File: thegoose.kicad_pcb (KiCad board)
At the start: 2 copper layers, 67 x 50 mm, 45 parts, among them U1 DRV8848, U2 DRV8848, U3 DRV8848, U4 AP64500SP-13

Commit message: Newify layout
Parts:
- removed R10, R11, R12, R7, R8, R9: .33, Resistor_SMD:R_0805_2012Metric_Pad1.20x1.40mm_HandSolder
- BT1: value XT30_SOLDER_CABLE -> XT60; footprint hexy:XT30_SolderPads_1x02_P5.00mm -> hexy:AMASS_XT60PW-M_1x02_P7.20mm_Horizontal
- moved S1 78.1 mm to (179.6, 117.8), turned to -90 degrees
- moved S6 76.3 mm to (128.8, 117.8), turned to -90 degrees
- moved C10 73.8 mm to (245.6, 74.0)
- moved C11 73.8 mm to (247.8, 74.0)
- moved C13 73.8 mm to (241.6, 73.7)
- moved C6 73.8 mm to (231.8, 73.7)
- moved C7 73.8 mm to (229.6, 73.7)
- moved C9 73.8 mm to (225.8, 73.7)
- moved C1 73.6 mm to (98.8, 99.6)
- moved C3 71.3 mm to (213.0, 73.2)
- moved C4 71.3 mm to (210.8, 73.2)
- moved M1 66.6 mm to (181.8, 54.0), turned to 180 degrees
- moved S2 66.3 mm to (169.4, 117.8), turned to -90 degrees
- moved S5 65.1 mm to (138.9, 117.8), turned to -90 degrees
- moved S3 59.3 mm to (159.3, 117.8), turned to -90 degrees
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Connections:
- U1 pad 10: /ESP_D4 -> /ESP_D16
- U1 pad 15: /ESP_D16 -> /ESP_D4
- U1 pad 16: /ESP_D17 -> /ESP_D15
- U1 pad 2: Net-(M2-OUT1) -> Net-(M1-OUT1)
- U1 pad 3: Net-(U1-AISEN) -> unconnected-(U1-AISEN-Pad3)
- U1 pad 4: Net-(M2-OUT2) -> Net-(M1-OUT2)
- U1 pad 5: Net-(M1-OUT1) -> Net-(M2-OUT1)
- U1 pad 6: Net-(U1-BISEN) -> unconnected-(U1-BISEN-Pad6)
- U1 pad 7: Net-(M1-OUT2) -> Net-(M2-OUT2)
- U1 pad 9: /ESP_D15 -> /ESP_D17
- U2 pad 10: /ESP_D18 -> /ESP_D19
- U2 pad 15: /ESP_D19 -> /ESP_D18
- U2 pad 16: /ESP_D21 -> /ESP_D5
- U2 pad 2: Net-(M4-OUT1) -> Net-(M3-OUT1)
- U2 pad 3: Net-(U2-AISEN) -> unconnected-(U2-AISEN-Pad3)
- U2 pad 4: Net-(M4-OUT2) -> Net-(M3-OUT2)
- U2 pad 5: Net-(M3-OUT1) -> Net-(M4-OUT1)
- U2 pad 6: Net-(U2-BISEN) -> unconnected-(U2-BISEN-Pad6)
- U2 pad 7: Net-(M3-OUT2) -> Net-(M4-OUT2)
- U2 pad 9: /ESP_D5 -> /ESP_D21
- U3 pad 2: Net-(M6-OUT1) -> Net-(M5-OUT1)
- U3 pad 3: Net-(U3-AISEN) -> unconnected-(U3-AISEN-Pad3)
- U3 pad 4: Net-(M6-OUT2) -> Net-(M5-OUT2)
- U3 pad 5: Net-(M5-OUT1) -> Net-(M6-OUT1)
- U3 pad 6: Net-(U3-BISEN) -> unconnected-(U3-BISEN-Pad6)
- U3 pad 7: Net-(M5-OUT2) -> Net-(M6-OUT2)
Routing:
- net +BATT: track 131.2 -> 1.01 mm, vias 4 -> 1
- net VCC: track 81.3 -> 0.00 mm
- net /ESP_D14: track 65.7 -> 0.00 mm, vias 3 -> 0
- net /ESP_D27: track 54.7 -> 0.00 mm, vias 1 -> 0
- net /ESP_D2: track 56.5 -> 18.8 mm, vias 4 -> 1
- net Net-(M3-OUT1): track 29.8 -> 0.00 mm, vias 2 -> 0
- net Net-(M4-OUT2): track 28.8 -> 0.00 mm, vias 3 -> 0
- net /ESP_D32: track 27.7 -> 0.00 mm, vias 1 -> 0
- net Net-(M4-OUT1): track 27.2 -> 0.00 mm, vias 1 -> 0
- net Net-(M5-OUT1): track 24.7 -> 0.00 mm, vias 1 -> 0
- net Net-(M6-OUT1): track 24.3 -> 0.00 mm, vias 2 -> 0
- net Net-(U3-VINT): track 23.6 -> 0.00 mm, vias 4 -> 0
- net Net-(M2-OUT1): track 27.9 -> 4.68 mm, vias 2 -> 0
- net Net-(M1-OUT1): track 29.9 -> 7.10 mm, vias 2 -> 0
- net Net-(U2-VINT): track 22.5 -> 0.00 mm, vias 4 -> 0
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- added copper zone on In2.Cu, net +BATT
- added copper zone on In1.Cu, net GND
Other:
- board size 67 x 50 mm -> 59.2 x 50 mm
- copper layers 2 -> 4

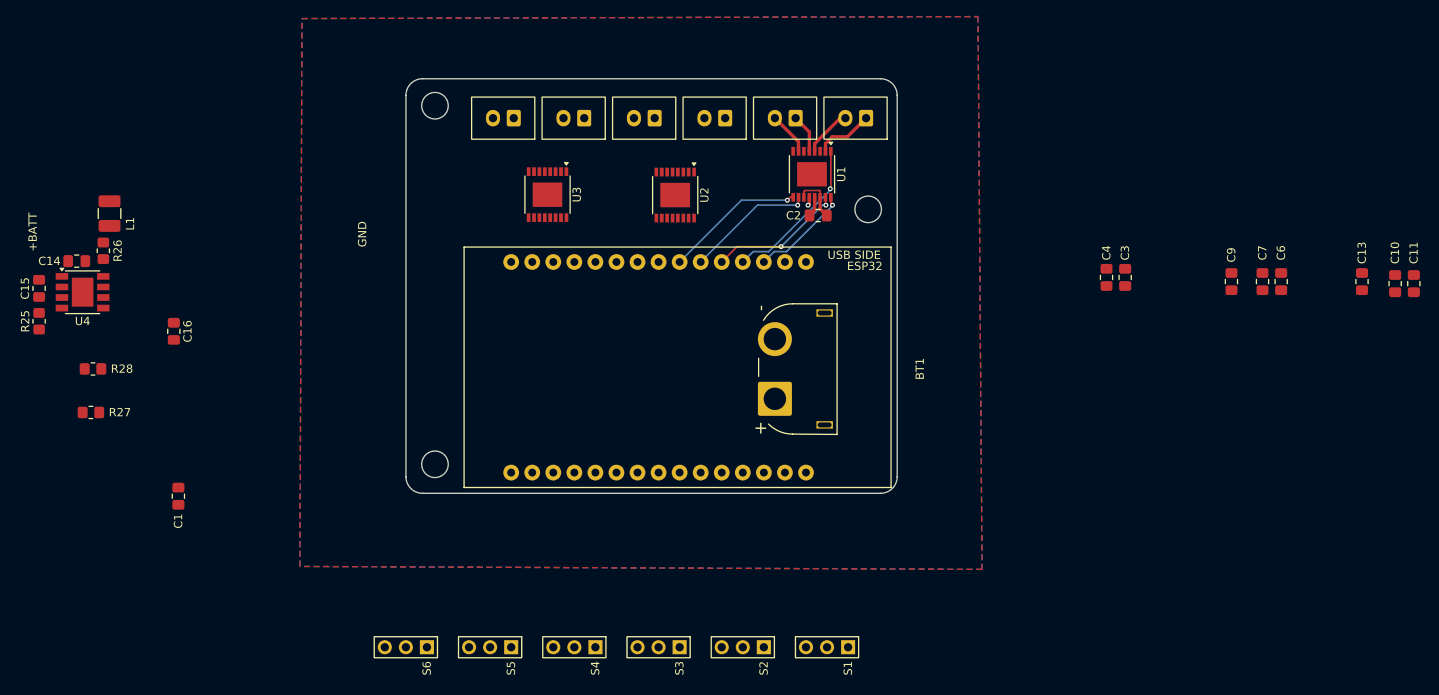
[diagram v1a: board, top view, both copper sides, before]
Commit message: Remove old separated gpio pins
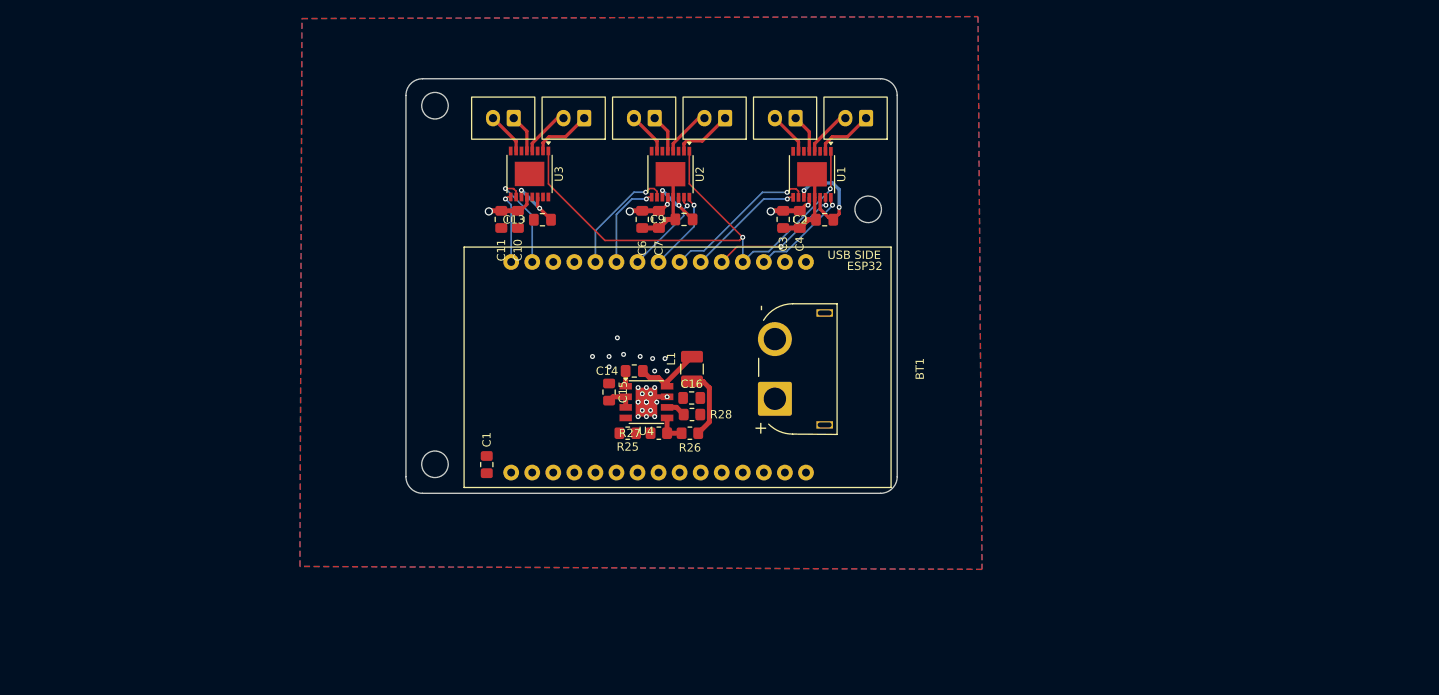
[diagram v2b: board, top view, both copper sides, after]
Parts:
- removed S1: IO_PORT_1, hexy:PinHeader_1x03_P2.54mm_Horizontal
- removed S2: IO_PORT_2, hexy:PinHeader_1x03_P2.54mm_Horizontal
- removed S3: IO_PORT_3, hexy:PinHeader_1x03_P2.54mm_Horizontal
- removed S4: IO_PORT_4, hexy:PinHeader_1x03_P2.54mm_Horizontal
- removed S5: IO_PORT_5, hexy:PinHeader_1x03_P2.54mm_Horizontal
- removed S6: IO_PORT_6, hexy:PinHeader_1x03_P2.54mm_Horizontal
- moved C11 110.3 mm to (137.8, 66.2), turned to -90 degrees
- moved C10 106.1 mm to (139.8, 66.2), turned to 90 degrees
- moved C13 99.1 mm to (142.7, 66.2), turned to 180 degrees
- moved C6 77.4 mm to (154.8, 66.2), turned to 90 degrees
- moved R26 74.1 mm to (160.5, 92.0), turned to 0 degrees
- moved C7 73.2 mm to (156.8, 66.2), turned to -90 degrees
- moved L1 72.7 mm to (160.8, 84.3), turned to -90 degrees
- moved R28 72.5 mm to (160.8, 89.8)
- moved R25 72.3 mm to (153.0, 92.0), turned to 180 degrees
- moved C15 69.9 mm to (150.8, 87.0), turned to -90 degrees
- moved U4 69.3 mm to (155.2, 88.2)
- moved R27 68.5 mm to (156.8, 92.0), turned to 0 degrees
- moved C14 68.5 mm to (153.8, 84.5)
- moved C9 66.5 mm to (159.8, 66.2), turned to 180 degrees
- moved C16 63.0 mm to (160.7, 87.8), turned to 0 degrees
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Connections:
- U1 pad 10: /ESP_D16 -> /ESP_D17
- U1 pad 9: /ESP_D17 -> /ESP_D16
- U2 pad 10: /ESP_D19 -> /ESP_D21
- U2 pad 9: /ESP_D21 -> /ESP_D19
- U3 pad 10: /ESP_D23 -> /ESP_D22
- U3 pad 9: /ESP_D22 -> /ESP_D23
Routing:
- net /ESP_D2: track 18.8 -> 65.4 mm, vias 1 -> 2
- net +BATT: track 1.01 -> 20.9 mm, vias 1 -> 5
- net GND: track 2.46 -> 21.8 mm, vias 0 -> 25
- net /ESP_D21: track 0.00 -> 14.1 mm, vias 0 -> 1
- net /ESP_D22: track 0.00 -> 12.3 mm, vias 0 -> 1
- net /ESP_D19: track 0.00 -> 10.8 mm, vias 0 -> 1
- net /ESP_D18: track 0.00 -> 10.5 mm, vias 0 -> 1
- net /ESP_D5: track 0.00 -> 9.82 mm, vias 0 -> 1
- net /ESP_D23: track 0.00 -> 8.62 mm, vias 0 -> 1
- net Net-(U4-SW): track 0.00 -> 8.50 mm
- net VCC: track 0.00 -> 8.46 mm
- net Net-(U3-VINT): track 0.00 -> 7.32 mm, vias 0 -> 2
- net Net-(U1-VINT): track 6.00 -> 13.2 mm, vias 0 -> 2
- net Net-(M5-OUT1): track 0.00 -> 7.19 mm
- net Net-(M3-OUT1): track 0.00 -> 7.16 mm
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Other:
- board text removed: "+BATT"
- board text removed: "C4"
- board text removed: "GND"

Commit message: Complete PCB
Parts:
- added GPIO1: Conn_06x3_Pin, hexy:PinHeader_3x06_P2.54mm_Horizontal, F.Cu at (140.5, 78.3)
- moved BT1 2.69 mm to (171.8, 78.2)
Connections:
- U1 pad 10: /ESP_D17 -> /ESP_D4
- U1 pad 15: /ESP_D4 -> /ESP_D12
- U1 pad 16: /ESP_D15 -> /ESP_D13
- U1 pad 9: /ESP_D16 -> /ESP_D15
- U2 pad 10: /ESP_D21 -> /ESP_D5
- U2 pad 15: /ESP_D18 -> /ESP_D17
- U2 pad 16: /ESP_D5 -> /ESP_D16
- U2 pad 9: /ESP_D19 -> /ESP_D18
- U3 pad 15: /ESP_D14 -> /ESP_D21
- U3 pad 16: /ESP_D27 -> /ESP_D19
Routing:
- net VCC: track 8.46 -> 68.2 mm
- net /ESP_D12: track 0.00 -> 38.5 mm, vias 0 -> 1
- net /ESP_D13: track 0.00 -> 37.5 mm, vias 0 -> 1
- net /ESP_D32: track 0.00 -> 33.3 mm
- net /ESP_D33: track 0.00 -> 32.6 mm
- net /ESP_D25: track 0.00 -> 32.0 mm
- net /ESP_D26: track 0.00 -> 31.3 mm
- net /ESP_D27: track 0.00 -> 30.7 mm
- net /ESP_D14: track 0.00 -> 28.7 mm
- net /ESP_D17: track 18.8 -> 8.35 mm
- net /ESP_D16: track 14.4 -> 8.38 mm
- net /ESP_D21: track 14.1 -> 10.5 mm
- net /ESP_D15: track 12.2 -> 9.56 mm, vias 1 -> 2
- net /ESP_D4: track 16.4 -> 14.6 mm, vias 2 -> 1
- net /ESP_D5: track 9.82 -> 11.6 mm
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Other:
- board size 59.2 x 50 mm -> 60.5 x 50 mm

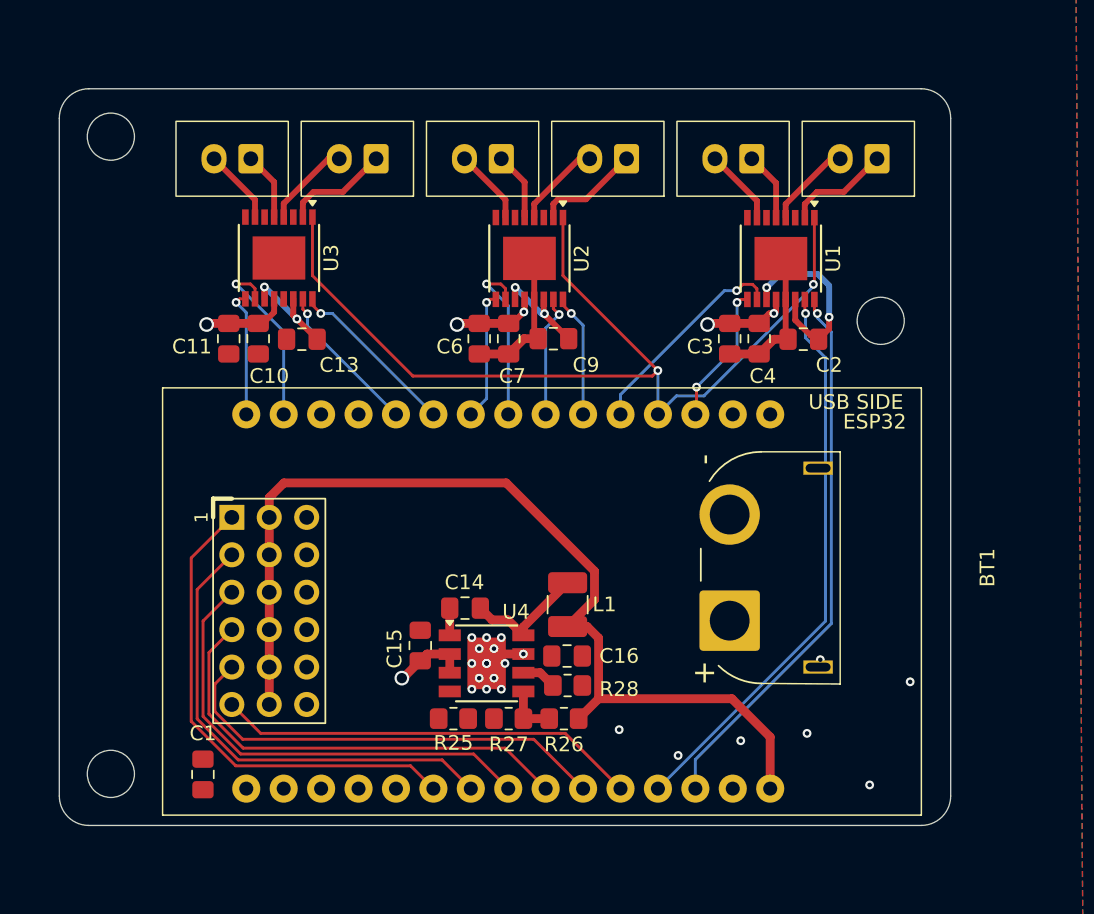
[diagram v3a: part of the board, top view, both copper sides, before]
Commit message: Add stitching vias and pass DRC
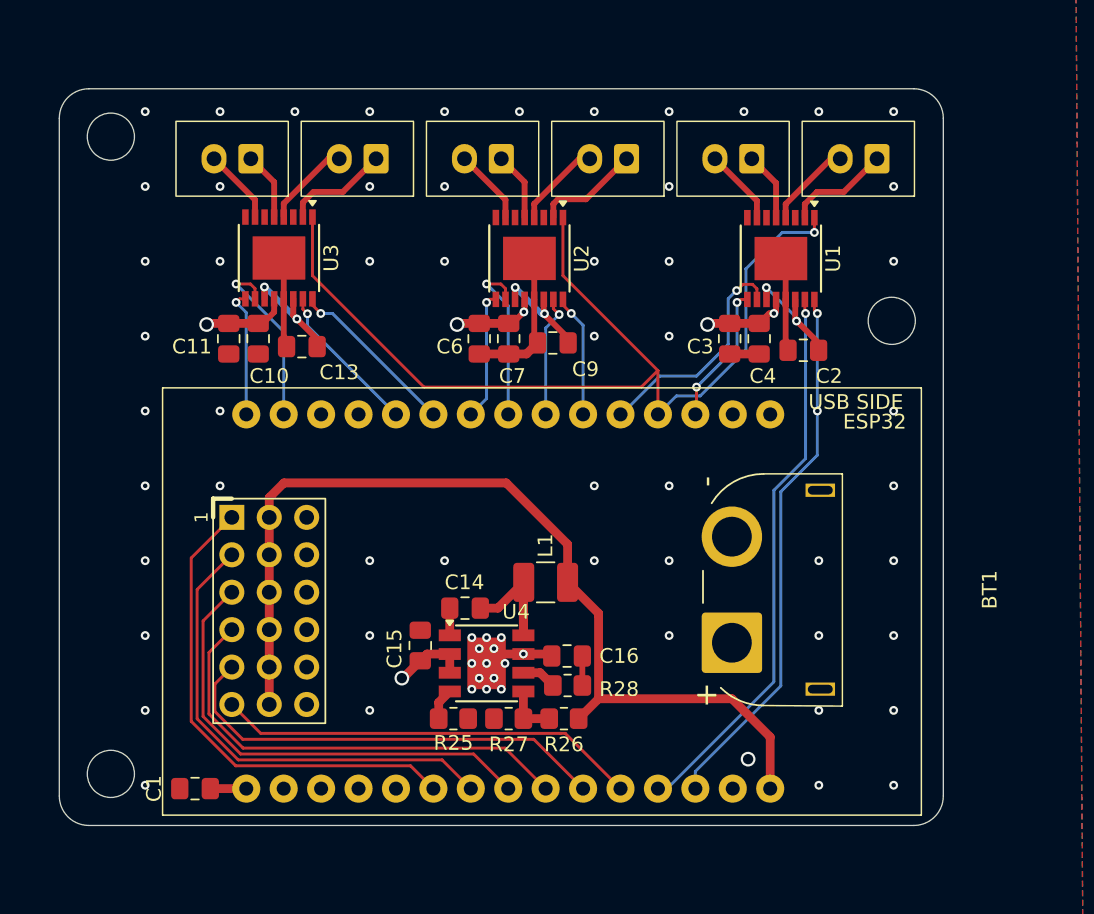
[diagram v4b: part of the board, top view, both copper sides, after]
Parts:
- moved L1 2.12 mm to (159.3, 82.8), turned to 0 degrees
- moved BT1 1.51 mm to (171.9, 79.7)
- moved C1 1.10 mm to (135.5, 96.8), turned to 180 degrees
- moved C2 0.75 mm to (176.8, 67.0)
- moved REF** 0.75 mm to (182.8, 65.0)
- moved C13 0.50 mm to (142.7, 66.8)
- moved C9 0.29 mm to (159.8, 66.5)
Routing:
- net Net-(U1-VINT): track 13.2 -> 7.79 mm
- net GND: track 21.8 -> 26.9 mm, vias 22 -> 69
- net Net-(ESP32-EN): track 0.00 -> 2.44 mm
- net VCC: track 68.2 -> 65.9 mm
- net Net-(U4-RT/CLK): track 0.00 -> 2.16 mm
- net Net-(C16-Pad2): track 0.00 -> 2.00 mm
- net /ESP_D2: track 65.4 -> 67.1 mm, vias 2 -> 1
- net Net-(U4-SW): track 8.50 -> 9.55 mm
- net /ESP_D4: track 14.6 -> 15.6 mm
- net /ESP_D13: track 37.5 -> 36.7 mm, vias 1 -> 2
- net /ESP_D12: track 38.5 -> 37.7 mm
- net Net-(U3-VINT): track 7.32 -> 7.82 mm
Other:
- board size 60.5 x 50 mm -> 60 x 50 mm

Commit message: Fix bad via
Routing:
- net /ESP_D13: vias 2 -> 1
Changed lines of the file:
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@@
-		(net 52)
-	)
-	(via
-		(at 177.700003 71.12)
-		(size 0.6)
-		(drill 0.3)
-		(layers "F.Cu" "B.Cu")
 		(net 52)
 	)

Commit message: Tackling warnings
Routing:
- net /ESP_D2: track 67.1 -> 66.4 mm
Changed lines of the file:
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@@
 	)
 	(via
-		(at 173 94.75)
+		(at 172 94.75)
 		(size 1)
 		(drill 0.7)
@@
 	)
 	(segment
-		(start 136.007 91.84896)
-		(end 138.55904 94.401)
-		(width 0.2)
-		(layer "F.Cu")
-		(net 29)
-	)
-	(segment
-		(start 138.55904 94.401)
-		(end 154.371 94.401)
+		(start 138.40804 94.25)
+		(end 154.22 94.25)
 		(width 0.2)
 		(layer "F.Cu")
@@
 	)
 	(segment
-		(start 154.371 94.401)
+		(start 154.22 94.25)
 		(end 156.72 96.75)
 		(width 0.2)
@@
 	)
 	(segment
+		(start 136.007 91.84896)
+		(end 138.40804 94.25)
+		(width 0.2)
+		(layer "F.Cu")
+		(net 29)
+	)
+	(segment
 		(start 136.5 96.75)
 		(end 138.94 96.75)
@@
 	)
 	(segment
+		(start 138.52814 93.803)
+		(end 156.313 93.803)
+		(width 0.2)
+		(layer "F.Cu")
+		(net 43)
+	)
+	(segment
+		(start 136.408 91.68286)
+		(end 138.52814 93.803)
+		(width 0.2)
+		(layer "F.Cu")
+		(net 43)
+	)
+	(segment
+		(start 136.408 87.512)
+		(end 136.408 91.68286)
+		(width 0.2)
+		(layer "F.Cu")
+		(net 43)
+	)
+	(segment
+		(start 156.313 93.803)
+		(end 159.26 96.75)
+		(width 0.2)
+		(layer "F.Cu")
+		(net 43)
+	)
+	(segment
 		(start 137.96 85.96)
 		(end 136.408 87.512)
@@
 	)
 	(segment
-		(start 156.51 94)
-		(end 159.26 96.75)
-		(width 0.2)
-		(layer "F.Cu")
-		(net 43)
-	)
-	(segment
-		(start 136.408 91.68286)
-		(end 138.72514 94)
-		(width 0.2)
-		(layer "F.Cu")
-		(net 43)
-	)
-	(segment
-		(start 136.408 87.512)
-		(end 136.408 91.68286)
-		(width 0.2)
-		(layer "F.Cu")
-		(net 43)
-	)
-	(segment
-		(start 138.72514 94)
-		(end 156.51 94)
-		(width 0.2)
-		(layer "F.Cu")
-		(net 43)
-	)
-	(segment
 		(start 173.6 62.825)
 		(end 173.299998 62.524998)
@@
 	)
 	(segment
+		(start 170 68.25)
+		(end 171.649 66.601)
+		(width 0.2)
+		(layer "B.Cu")
+		(net 44)
+	)
+	(segment
+		(start 164.4 71.35)
+		(end 167.5 68.25)
+		(width 0.2)
+		(layer "B.Cu")
+		(net 44)
+	)
+	(segment
 		(start 171.649 66.601)
 		(end 171.649 63.501057)
@@
 	)
 	(segment
+		(start 164.34 71.35)
+		(end 164.4 71.35)
+		(width 0.2)
+		(layer "B.Cu")
+		(net 44)
+	)
+	(segment
 		(start 172.19955 62.950507)
 		(end 172.221445 62.950507)
@@
 	)
 	(segment
-		(start 164.34 71.35)
-		(end 164.4 71.35)
-		(width 0.2)
-		(layer "B.Cu")
-		(net 44)
-	)
-	(segment
-		(start 167 68.75)
-		(end 169.5 68.75)
-		(width 0.2)
-		(layer "B.Cu")
-		(net 44)
-	)
-	(segment
-		(start 169.5 68.75)
-		(end 171.649 66.601)
-		(width 0.2)
-		(layer "B.Cu")
-		(net 44)
-	)
-	(segment
-		(start 164.4 71.35)
-		(end 167 68.75)
+		(start 167.5 68.25)
+		(end 170 68.25)
 		(width 0.2)
 		(layer "B.Cu")
@@
 	)
 	(segment
+		(start 137.96 80.88)
+		(end 135.606 83.234)
+		(width 0.2)
+		(layer "F.Cu")
+		(net 49)
+	)
+	(segment
+		(start 135.606 92.01506)
+		(end 138.24194 94.651)
+		(width 0.2)
+		(layer "F.Cu")
+		(net 49)
+	)
+	(segment
 		(start 135.606 83.234)
 		(end 135.606 92.01506)
@@
 	)
 	(segment
-		(start 138.39294 94.802)
-		(end 152.232 94.802)
+		(start 138.24194 94.651)
+		(end 152.081 94.651)
 		(width 0.2)
 		(layer "F.Cu")
@@
 	)
 	(segment
-		(start 152.232 94.802)
+		(start 152.081 94.651)
 		(end 154.18 96.75)
 		(width 0.2)
@@
 	)
 	(segment
-		(start 137.96 80.88)
-		(end 135.606 83.234)
-		(width 0.2)
-		(layer "F.Cu")
-		(net 49)
-	)
-	(segment
-		(start 135.606 92.01506)
-		(end 138.39294 94.802)
-		(width 0.2)
-		(layer "F.Cu")
-		(net 49)
+		(start 143.4325 57.96)
+		(end 143.4325 62.1825)
+		(width 0.2)
+		(layer "F.Cu")
+		(net 50)
 	)
 	(segment
@@
 	)
 	(segment
-		(start 165.75 69.5)
+		(start 166.75 68.5)
 		(end 166.875 68.375)
 		(width 0.2)
@@
 	)
 	(segment
-		(start 143.4325 61.9325)
-		(end 151 69.5)
+		(start 143.4325 62.1825)
+		(end 149.75 68.5)
 		(width 0.2)
 		(layer "F.Cu")
@@
 	)
 	(segment
-		(start 151 69.5)
-		(end 165.75 69.5)
-		(width 0.2)
-		(layer "F.Cu")
-		(net 50)
-	)
-	(segment
-		(start 143.4325 57.96)
-		(end 143.4325 61.9325)
+		(start 149.75 68.5)
+		(end 166.75 68.5)
 		(width 0.2)
 		(layer "F.Cu")
@@
 	)
 	(segment
-		(start 150.093 95.203)
+		(start 135.205 92.18116)
+		(end 138.07584 95.052)
+		(width 0.2)
+		(layer "F.Cu")
+		(net 58)
+	)
+	(segment
+		(start 149.942 95.052)
 		(end 151.64 96.75)
+		(width 0.2)
+		(layer "F.Cu")
+		(net 58)
+	)
+	(segment
+		(start 135.205 81.095)
+		(end 135.205 92.18116)
+		(width 0.2)
+		(layer "F.Cu")
+		(net 58)
+	)
+	(segment
+		(start 138.07584 95.052)
+		(end 149.942 95.052)
 		(width 0.2)
 		(layer "F.Cu")
@@
 	)
 	(segment
-		(start 135.205 81.095)
-		(end 135.205 92.18116)
-		(width 0.2)
-		(layer "F.Cu")
-		(net 58)
-	)
-	(segment
-		(start 135.205 92.18116)
-		(end 138.22684 95.203)
-		(width 0.2)
-		(layer "F.Cu")
-		(net 58)
-	)
-	(segment
-		(start 138.22684 95.203)
-		(end 150.093 95.203)
-		(width 0.2)
-		(layer "F.Cu")
-		(net 58)
-	)
-	(segment
 		(start 137.96 88.5)
 		(end 136.809 89.651)
@@
 	)
 	(segment
+		(start 169.99825 68.99825)
+		(end 169.5 69.4965)
+		(width 0.2)
+		(layer "F.Cu")
+		(net 60)
+	)
+	(segment
 		(start 169.5 69.4965)
 		(end 169.5 71.27)
@@
 	)
 	(via
-		(at 169.5 69.4965)
+		(at 169.99825 68.99825)
 		(size 0.6)
 		(drill 0.3)
@@
 	)
 	(segment
-		(start 172.25 63.75)
+		(start 172.25 66.7465)
+		(end 172.25 63.75)
+		(width 0.2)
+		(layer "B.Cu")
+		(net 60)
+	)
+	(segment
+		(start 169.99825 68.99825)
 		(end 172.25 66.7465)
 		(width 0.2)
 		(layer "B.Cu")
-		(net 60)
-	)
-	(segment
-		(start 172.25 66.7465)
-		(end 169.5 69.4965)
-		(width 0.2)
-		(layer "B.Cu")

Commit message: Update LCSC part numbers
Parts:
- L1: footprint Inductor_SMD:L_1210_3225Metric_Pad1.42x2.65mm_HandSolder -> Inductor_SMD_Wurth:L_Wurth_WE-LQSH-4020
- moved L1 1.34 mm to (160.5, 83.2)
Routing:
- net GND: track 26.9 -> 36.7 mm, vias 69 -> 54
- net Net-(U4-SW): track 9.55 -> 8.24 mm
